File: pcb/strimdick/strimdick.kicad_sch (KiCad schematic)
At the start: 4 parts, among them U1 ProMicro

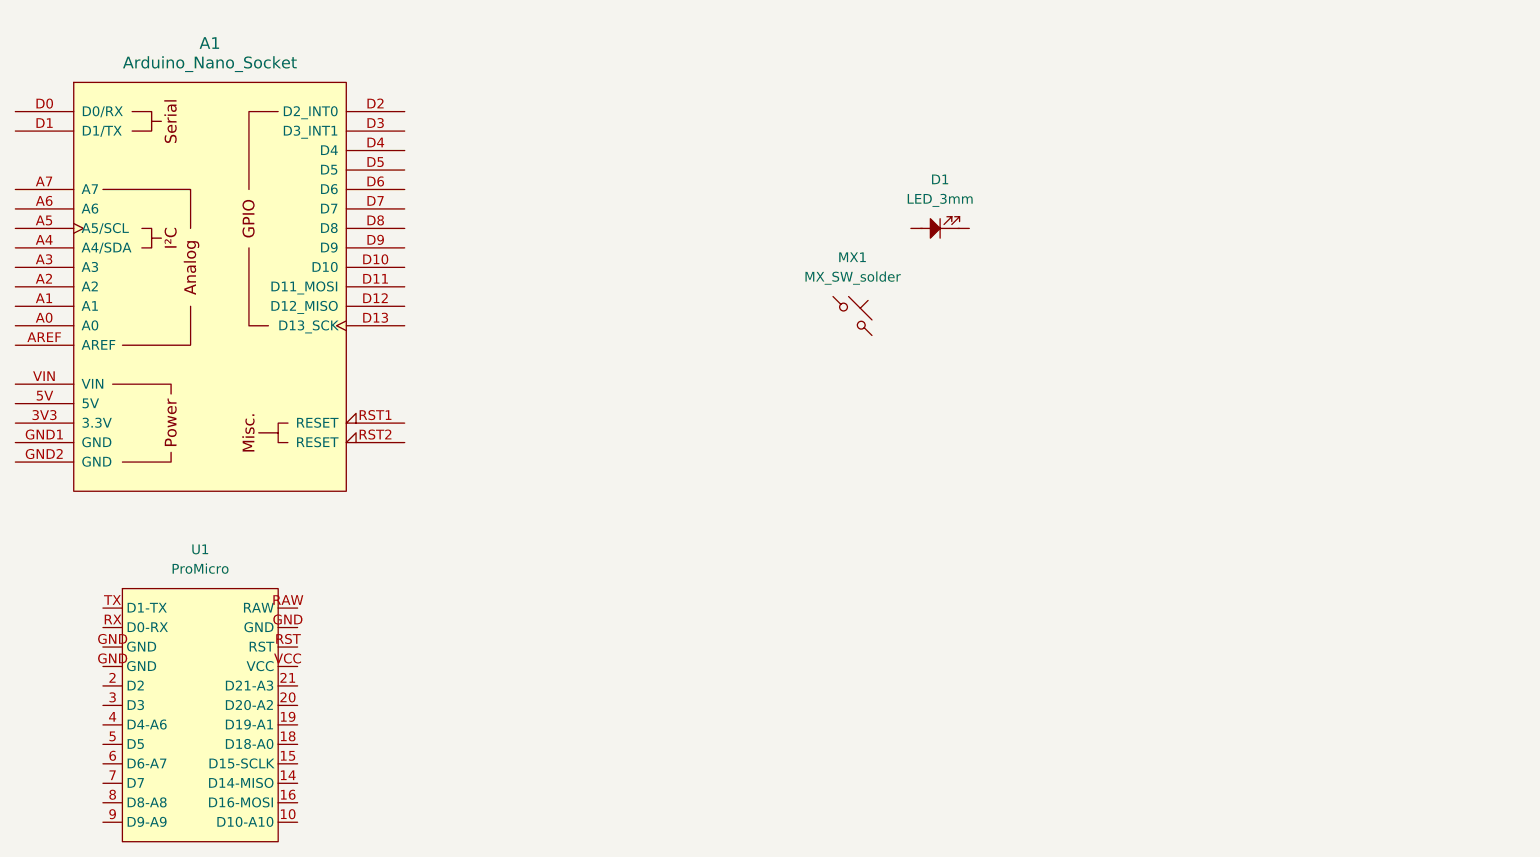
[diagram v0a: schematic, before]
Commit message: Okay, got the schematic done, and a basic layout with things all stacked up, it's a bit tight
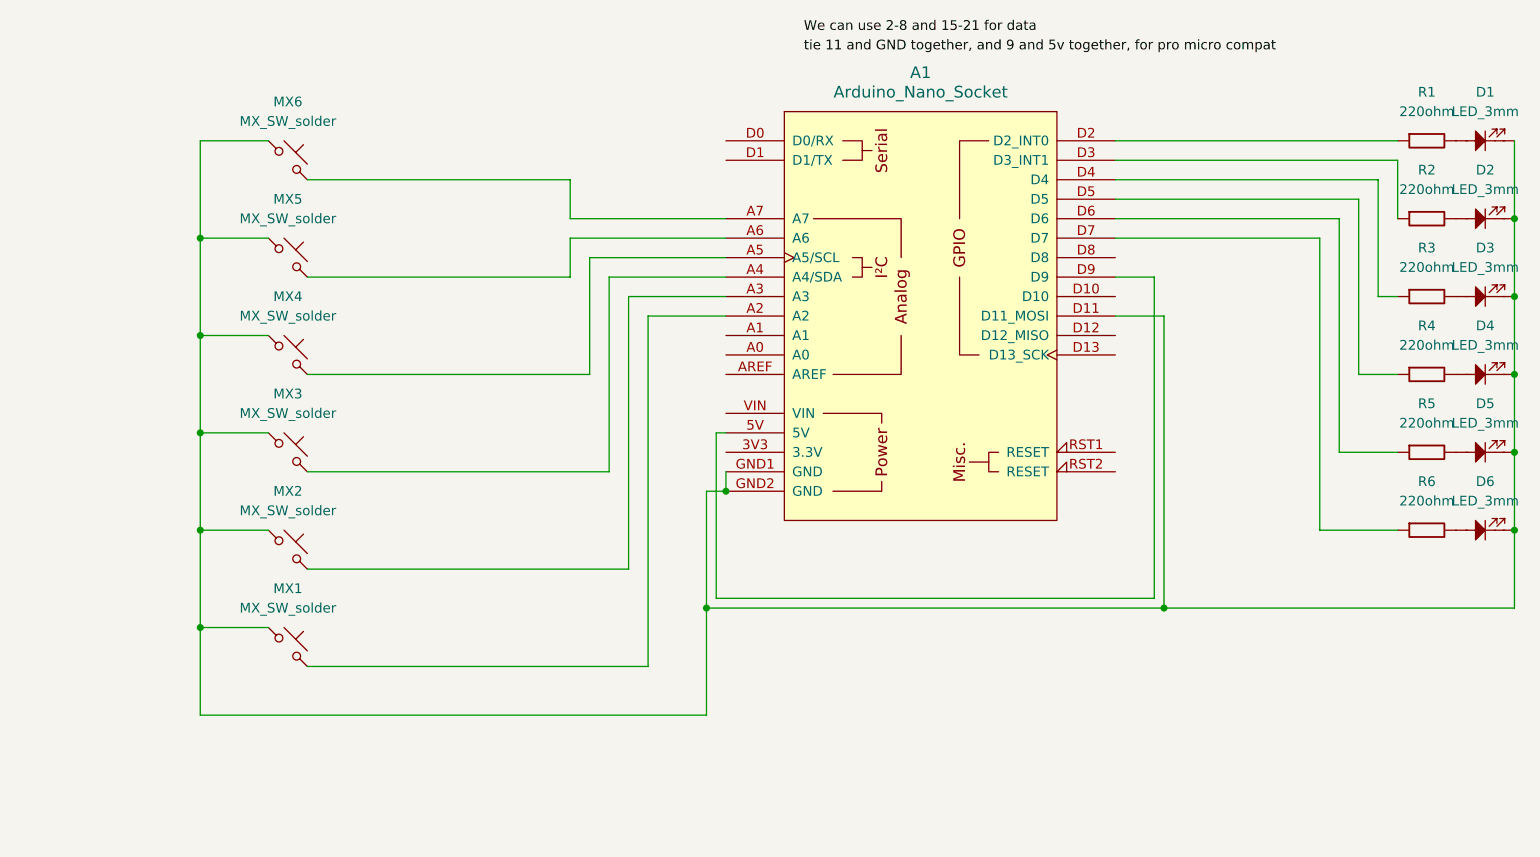
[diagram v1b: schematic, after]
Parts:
- removed U1: ProMicro, Neko:ProMicro_USBup, symbol Neko:Arduino_ProMicro
- added D2, D3, D4, D5, D6: LED_3mm, PCM_marbastlib-mx:LED_MX_3mm, symbol PCM_SL_Devices:LED_3mm
- added MX1, MX2, MX3, MX4, MX5: MX_SW_solder, PCM_marbastlib-mx:SW_MX_1u, symbol PCM_marbastlib-mx:MX_SW_solder
- added R1, R2, R3, R4, R5, R6: 220ohm, Resistor_THT:R_Axial_DIN0207_L6.3mm_D2.5mm_P10.16mm_Horizontal, symbol PCM_SL_Resistors:220ohm
- D1: footprint LED_THT:LED_D3.0mm -> PCM_marbastlib-mx:LED_MX_3mm
- renumbered MX1 to MX6
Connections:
- net at MX6.1: now also A1.D11 (D11_MOSI), A1.GND1 (GND), A1.GND2 (GND), D1.1, D2.1, D3.1, D4.1, D5.1, D6.1, MX1.1, MX2.1, MX3.1, MX4.1, MX5.1
- net at MX6.2: now also A1.A7
- net at A1.5V: now also A1.D9
- net at A1.A2: now also MX1.2
- net at A1.A3: now also MX2.2
- net at A1.A4 (A4/SDA): now also MX3.2
- net at A1.A5 (A5/SCL): now also MX4.2
- net at A1.A6: now also MX5.2
- net at A1.D2 (D2_INT0): now also R1.1
- net at A1.D3 (D3_INT1): now also R2.1
- net at A1.D4: now also R3.1
- net at A1.D5: now also R4.1
- net at A1.D6: now also R5.1
- net at A1.D7: now also R6.1
- net at D1.2: now also R1.2
- new net: D4.2, R4.2
- new net: D6.2, R6.2
- new net: D2.2, R2.2
- new net: D3.2, R3.2
- new net: D5.2, R5.2
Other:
- moved on the sheet: A1, D1, MX6

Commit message: Routing, some silkscreen instructions.
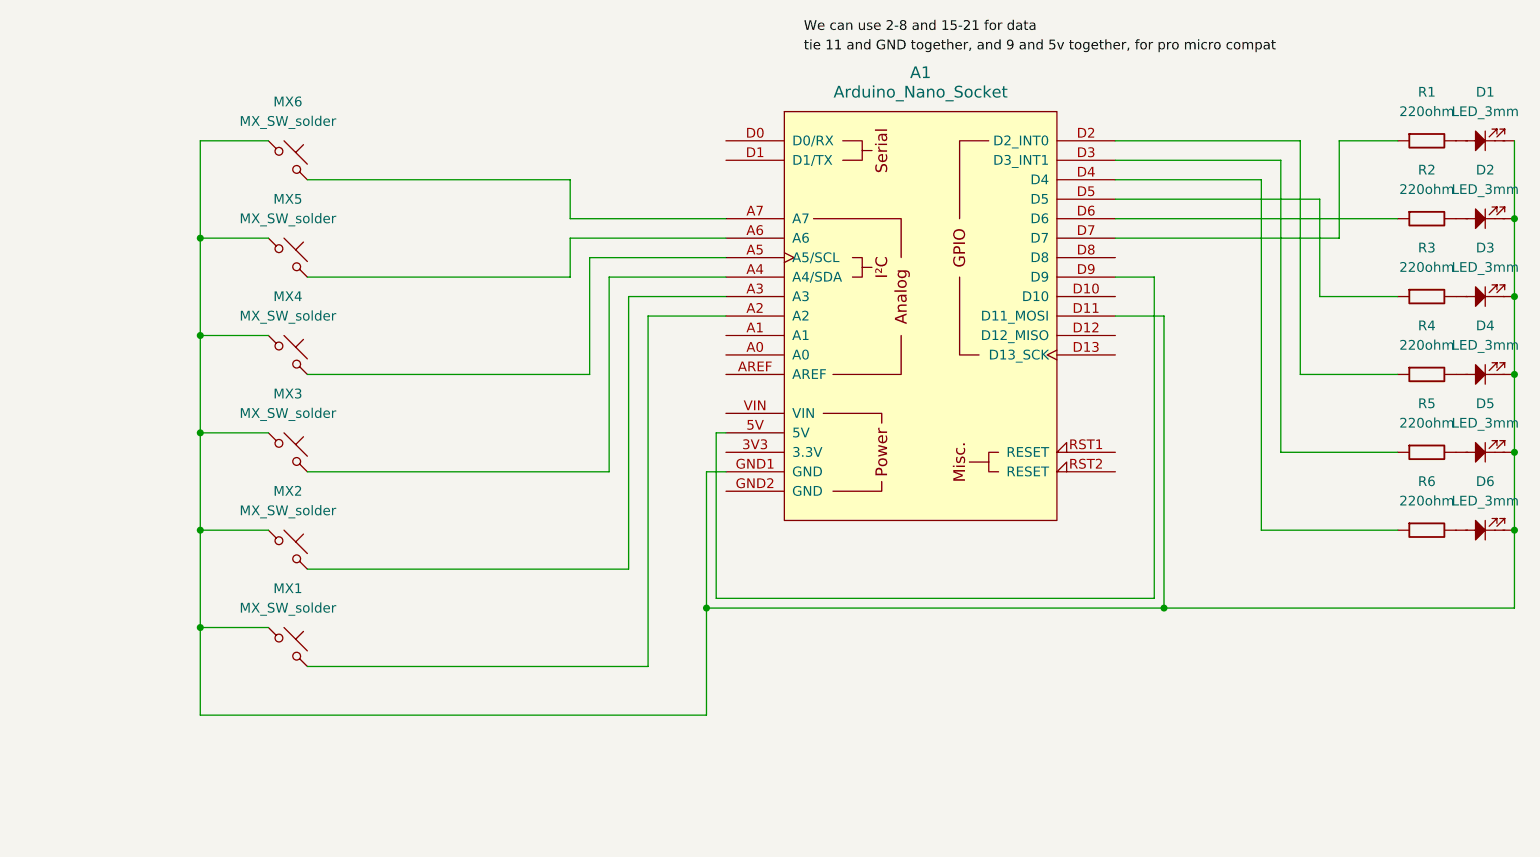
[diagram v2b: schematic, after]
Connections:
- net at R4.1: now also A1.D2 (D2_INT0); no longer A1.D5
- net at A1.D11 (D11_MOSI), A1.GND1 (GND), D1.1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: no longer A1.GND2 (GND)
- net at R3.1: now also A1.D5; no longer A1.D4
- net at R5.1: now also A1.D3 (D3_INT1); no longer A1.D6
- net at R1.1: now also A1.D7; no longer A1.D2 (D2_INT0)
- net at R2.1: now also A1.D6; no longer A1.D3 (D3_INT1)
- net at R6.1: now also A1.D4; no longer A1.D7
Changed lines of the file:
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@@
-	)
-	(junction
-		(at 109.22 81.28)
-		(diameter 0)
-		(color 0 0 0 0)
 	)
 	(junction
@@
 	(wire
 		(pts
-			(xy 160.02 40.64) (xy 194.31 40.64)
-		)
-		(stroke
-			(width 0)
-			(type default)
-		)
-	)
-	(wire
-		(pts
 			(xy 93.98 53.34) (xy 109.22 53.34)
 		)
@@
 	(wire
 		(pts
-			(xy 191.77 66.04) (xy 196.85 66.04)
+			(xy 186.69 43.18) (xy 186.69 55.88)
 		)
 		(stroke
@@
 	(wire
 		(pts
-			(xy 189.23 45.72) (xy 189.23 76.2)
+			(xy 160.02 45.72) (xy 196.85 45.72)
 		)
 		(stroke
@@
 	(wire
 		(pts
-			(xy 194.31 40.64) (xy 194.31 55.88)
+			(xy 179.07 40.64) (xy 179.07 86.36)
 		)
 		(stroke
@@
 	(wire
 		(pts
+			(xy 179.07 86.36) (xy 196.85 86.36)
+		)
+		(stroke
+			(width 0)
+			(type default)
+		)
+	)
+	(wire
+		(pts
+			(xy 160.02 38.1) (xy 181.61 38.1)
+		)
+		(stroke
+			(width 0)
+			(type default)
+		)
+	)
+	(wire
+		(pts
 			(xy 40.64 86.36) (xy 40.64 73.66)
 		)
@@
 	(wire
 		(pts
-			(xy 160.02 38.1) (xy 196.85 38.1)
+			(xy 160.02 43.18) (xy 186.69 43.18)
 		)
 		(stroke
@@
 	(wire
 		(pts
-			(xy 191.77 43.18) (xy 191.77 66.04)
-		)
-		(stroke
-			(width 0)
-			(type default)
-		)
-	)
-	(wire
-		(pts
-			(xy 160.02 48.26) (xy 186.69 48.26)
-		)
-		(stroke
-			(width 0)
-			(type default)
-		)
-	)
-	(wire
-		(pts
 			(xy 96.52 55.88) (xy 109.22 55.88)
 		)
@@
 	(wire
 		(pts
-			(xy 160.02 35.56) (xy 196.85 35.56)
-		)
-		(stroke
-			(width 0)
-			(type default)
-		)
-	)
-	(wire
-		(pts
-			(xy 189.23 76.2) (xy 196.85 76.2)
-		)
-		(stroke
-			(width 0)
-			(type default)
-		)
-	)
-	(wire
-		(pts
-			(xy 106.68 81.28) (xy 109.22 81.28)
-		)
-		(stroke
-			(width 0)
-			(type default)
-		)
-	)
-	(wire
-		(pts
 			(xy 40.64 99.06) (xy 40.64 86.36)
 		)
@@
 	(wire
 		(pts
+			(xy 181.61 38.1) (xy 181.61 76.2)
+		)
+		(stroke
+			(width 0)
+			(type default)
+		)
+	)
+	(wire
+		(pts
 			(xy 212.09 96.52) (xy 166.37 96.52)
 		)
@@
 	(wire
 		(pts
+			(xy 189.23 48.26) (xy 189.23 35.56)
+		)
+		(stroke
+			(width 0)
+			(type default)
+		)
+	)
+	(wire
+		(pts
 			(xy 88.9 40.64) (xy 88.9 45.72)
 		)
@@
 	(wire
 		(pts
+			(xy 184.15 66.04) (xy 196.85 66.04)
+		)
+		(stroke
+			(width 0)
+			(type default)
+		)
+	)
+	(wire
+		(pts
 			(xy 40.64 99.06) (xy 49.53 99.06)
 		)
@@
 	(wire
 		(pts
+			(xy 181.61 76.2) (xy 196.85 76.2)
+		)
+		(stroke
+			(width 0)
+			(type default)
+		)
+	)
+	(wire
+		(pts
 			(xy 40.64 48.26) (xy 49.53 48.26)
 		)
@@
 	(wire
 		(pts
-			(xy 160.02 45.72) (xy 189.23 45.72)
-		)
-		(stroke
-			(width 0)
-			(type default)
-		)
-	)
-	(wire
-		(pts
 			(xy 165.1 95.25) (xy 165.1 53.34)
 		)
@@
 	(wire
 		(pts
-			(xy 109.22 78.74) (xy 109.22 81.28)
+			(xy 160.02 40.64) (xy 179.07 40.64)
 		)
 		(stroke
@@
 	(wire
 		(pts
-			(xy 194.31 55.88) (xy 196.85 55.88)
-		)
-		(stroke
-			(width 0)
-			(type default)
-		)
-	)
-	(wire
-		(pts
 			(xy 166.37 58.42) (xy 160.02 58.42)
 		)
@@
 	(wire
 		(pts
+			(xy 184.15 35.56) (xy 184.15 66.04)
+		)
+		(stroke
+			(width 0)
+			(type default)
+		)
+	)
+	(wire
+		(pts
 			(xy 212.09 35.56) (xy 212.09 45.72)
 		)
@@
 	(wire
 		(pts
+			(xy 160.02 48.26) (xy 189.23 48.26)
+		)
+		(stroke
+			(width 0)
+			(type default)
+		)
+	)
+	(wire
+		(pts
 			(xy 40.64 48.26) (xy 40.64 35.56)
 		)
@@
 	(wire
 		(pts
-			(xy 186.69 48.26) (xy 186.69 86.36)
-		)
-		(stroke
-			(width 0)
-			(type default)
-		)
-	)
-	(wire
-		(pts
 			(xy 107.95 95.25) (xy 165.1 95.25)
 		)
@@
 	(wire
 		(pts
-			(xy 186.69 86.36) (xy 196.85 86.36)
-		)
-		(stroke
-			(width 0)
-			(type default)
-		)
-	)
-	(wire
-		(pts
 			(xy 166.37 96.52) (xy 166.37 58.42)
 		)
@@
 	(wire
 		(pts
-			(xy 160.02 43.18) (xy 191.77 43.18)
+			(xy 160.02 35.56) (xy 184.15 35.56)
 		)
 		(stroke
@@
 	(wire
 		(pts
-			(xy 106.68 81.28) (xy 106.68 96.52)
-		)
-		(stroke
-			(width 0)
-			(type default)
-		)
-	)
-	(wire
-		(pts
-			(xy 196.85 38.1) (xy 196.85 45.72)
+			(xy 189.23 35.56) (xy 196.85 35.56)
+		)
+		(stroke
+			(width 0)
+			(type default)
+		)
+	)
+	(wire
+		(pts
+			(xy 109.22 78.74) (xy 106.68 78.74)
+		)
+		(stroke
+			(width 0)
+			(type default)
+		)
+	)
+	(wire
+		(pts
+			(xy 106.68 78.74) (xy 106.68 96.52)
 		)
 		(stroke
@@
 		)
 		(stroke
+			(width 0)
+			(type default)
+		)
+	)
+	(wire
+		(pts
+			(xy 186.69 55.88) (xy 196.85 55.88)
+		)
+		(stroke

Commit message: trying this 'add fill' thing
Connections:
- net GND: now reaches A1.D11 (D11_MOSI), A1.GND1 (GND), D1.1, D2.1, D3.1, D4.1, D5.1, D6.1, MX1.1, MX2.1, MX3.1, MX4.1, MX5.1, MX6.1
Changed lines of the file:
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@@
+	)
+	(junction
+		(at 113.03 96.52)
+		(diameter 0)
+		(color 0 0 0 0)
 	)
 	(junction
@@
 	(wire
 		(pts
-			(xy 106.68 96.52) (xy 166.37 96.52)
+			(xy 106.68 96.52) (xy 113.03 96.52)
 		)
 		(stroke
@@
 		(pts
 			(xy 99.06 58.42) (xy 109.22 58.42)
+		)
+		(stroke
+			(width 0)
+			(type default)
+		)
+	)
+	(wire
+		(pts
+			(xy 113.03 96.52) (xy 166.37 96.52)
 		)
 		(stroke
@@
 					(unit 1)
 				)
+			)
+		)
+	)
+	(symbol
+		(lib_id "power:GND")
+		(at 113.03 96.52 0)
+		(unit 1)
+		(exclude_from_sim no)
+		(in_bom yes)
+		(on_board yes)
+		(dnp no)
+		(fields_autoplaced yes)
+		(property "Reference" "#PWR01"
+			(at 113.03 102.87 0)
+			(effects
+				(font
+					(size 1.27 1.27)
+				)
+				(hide yes)
+			)
+		)
+		(property "Value" "GND"
+			(at 113.03 101.6 0)
+			(effects
+				(font
+					(size 1.27 1.27)
+				)
+			)
+		)
+		(property "Footprint" ""
+			(at 113.03 96.52 0)
+			(effects
+				(font
+					(size 1.27 1.27)
+				)
+				(hide yes)
+			)
+		)
+		(property "Datasheet" ""
+			(at 113.03 96.52 0)
+			(effects
+				(font
+					(size 1.27 1.27)
+				)
+				(hide yes)
+			)
+		)
+		(property "Description" "Power symbol creates a global label with name \"GND\" , ground"
+			(at 113.03 96.52 0)
+			(effects
+				(font
+					(size 1.27 1.27)
+				)
+				(hide yes)
+			)
+		)
+		(pin "1"
+		)
+		(instances
+			(project ""
+				(path "/e2f8e7b6-0a13-4122-a7f5-bc56009a9446"
+					(reference "#PWR01")
+					(unit 1)
+				)
